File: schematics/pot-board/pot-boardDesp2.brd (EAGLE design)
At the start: 86.4 x 41.9 mm, 15 parts, among them J3 POWER_JACKPTH_LOCK, U1 SPARKFUN_PRO_MICRO, U2 DC-DC-STEP-DOWN-LM2596

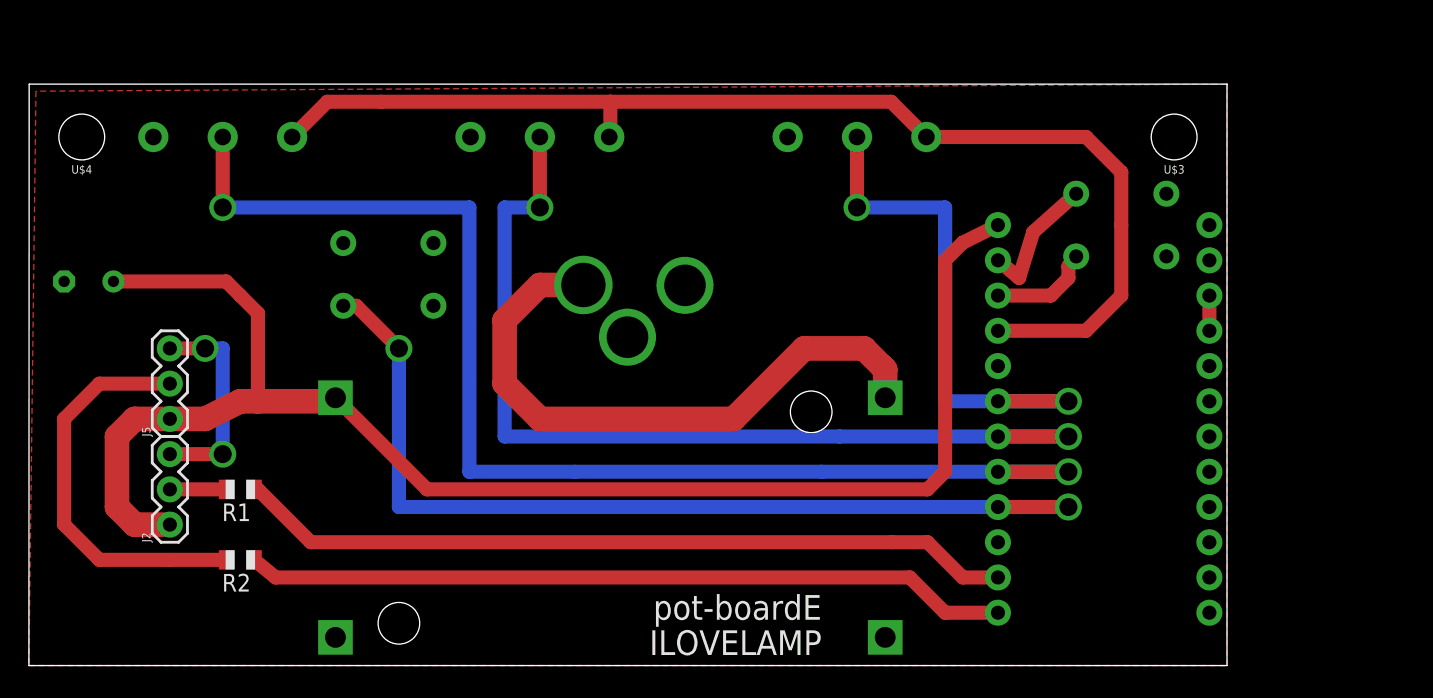
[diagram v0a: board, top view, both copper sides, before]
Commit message: added esp pot boards
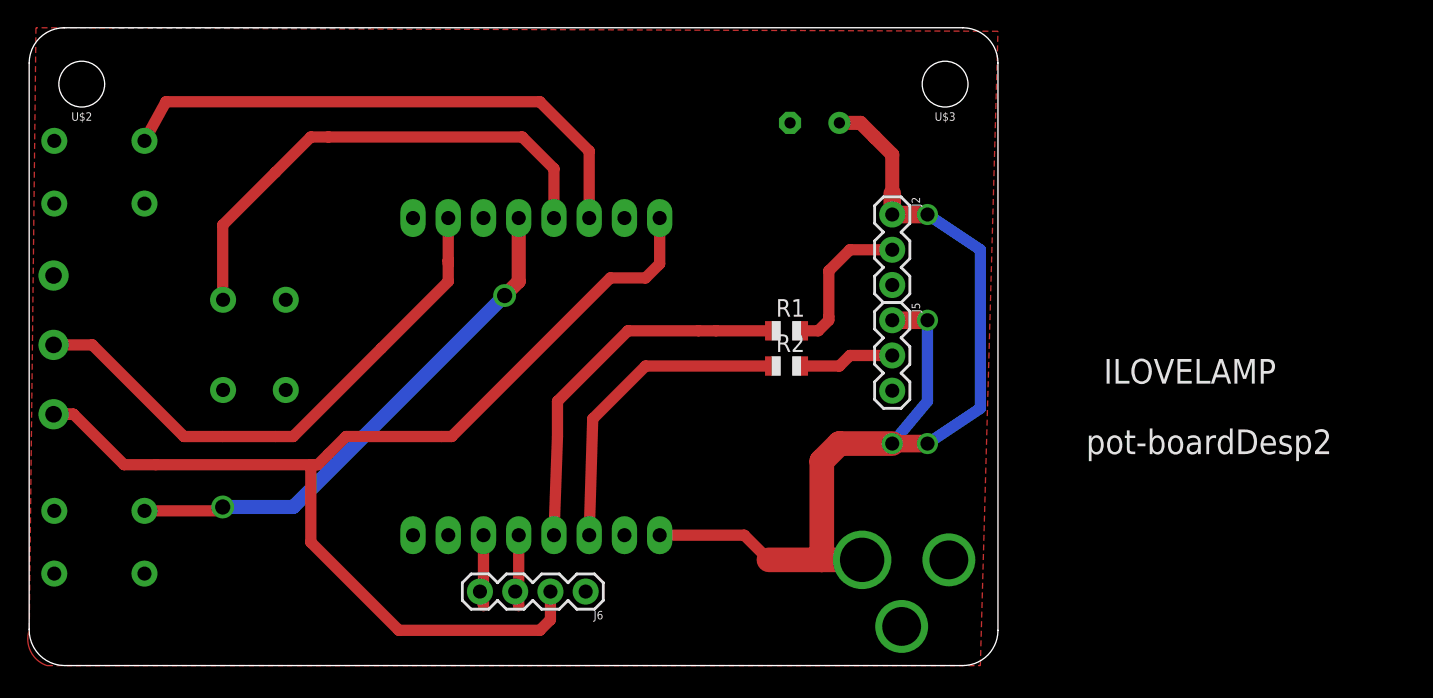
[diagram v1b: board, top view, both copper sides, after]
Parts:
- removed J3: POWER_JACKPTH_LOCK, SparkFun-Connectors:POWER_JACK_PTH_LOCK
- removed R4, R5: (no value), pot:3RP/1610N
- removed S4: tact6mm, SparkFun-Switches:TACTILE_SWITCH_PTH_6.0MM
- removed U$4: (no value), SparkFun-Hardware:STAND-OFF
- removed U1: SPARKFUN_PRO_MICRO, SparkFun-Boards:SPARKFUN_PRO_MICRO
- removed U2: DC-DC-STEP-DOWN-LM2596, diy-modules:DC-DC-STEP-DOWN-LM2596
- added CN1: (no value), adafruit:DCJACK_2MM_PTH
- added J6: (no value), SparkFun-Connectors:1X04
- added S2, S3: tact6mm, SparkFun-Switches:TACTILE_SWITCH_PTH_6.0MM
- added U$2: (no value), SparkFun-Hardware:STAND-OFF
- added WEMOS1: (no value), esp8266modules:WEMOS-D1-MINI
- moved J2 56.7 mm to (62.2, 32.5), turned to 270 degrees
- moved C2 53.6 mm to (56.6, 39.1)
- moved J5 52.6 mm to (62.2, 24.9), turned to 270 degrees
- moved R2 41.8 mm to (54.6, 21.6), turned to 0 degrees
- moved R1 41.0 mm to (54.6, 24.1), turned to 0 degrees
- moved S1 28.4 mm to (5.08, 8.89), turned to 0 degrees
- moved R3 19.3 mm to (1.78, 23.1), turned to 90 degrees
- moved U$3 16.9 mm to (66.0, 41.9)
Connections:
- removed net A1: R4.2, U1.18
- removed net A2: R5.2, U1.19
- removed net N$1: J3.PWR, U2.IN+
- removed net N$5: U1.12
- removed net N$6: U1.15
- removed net RESET: S4.1, U1.22
- removed net RR: U1.7
- removed net VCC: R3.3, R4.3, R5.3, U1.21
- new net +3V3: J6.2, R3.1, WEMOS1.3V3
- new net BUTT2: S2.1, WEMOS1.D6
- new net BUTT3: S3.1, WEMOS1.D7
- net A0: now also WEMOS1.A0; no longer U1.17
- net BUTT1: now also WEMOS1.D5; no longer U1.16
- net GND: now also CN1.GND, CN1.GNDBREAK, J6.1, R3.3, S2.3, S3.3, WEMOS1.GND; no longer J3.GND, J3.GNDBREAK, R3.1, R4.1, R5.1, S4.3, U1.23, U1.3, U1.4, U2.IN-, U2.OUT-
- net LED1: now also WEMOS1.D4; no longer U1.13
- net LED2: now also WEMOS1.D3; no longer U1.14
- net SCL: now also J6.4, WEMOS1.D1; no longer U1.6
- net SDA: now also J6.3, WEMOS1.D2; no longer U1.5
- net VIN: now also CN1.PWR, WEMOS1.5V; no longer U1.24, U2.OUT+
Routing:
- net VCC: track 84.4 -> 0.00 mm
- net +3V3: track 0.00 -> 83.0 mm
- net A1: track 69.9 -> 0.00 mm, vias 2 -> 0
- net A0: track 90.2 -> 40.6 mm, vias 2 -> 0
- net N$1: track 44.6 -> 0.00 mm
- net BUTT3: track 0.00 -> 40.0 mm
- net A2: track 39.4 -> 0.00 mm, vias 2 -> 0
- net BUTT2: track 0.00 -> 36.4 mm
- net VIN: track 113.7 -> 77.7 mm, vias 0 -> 4
- net LED1: track 55.1 -> 22.9 mm
- net BUTT1: track 70.1 -> 38.6 mm
- net LED2: track 56.2 -> 27.3 mm
- net GND: track 27.4 -> 0.00 mm, vias 2 -> 0
- net LED1O: track 29.0 -> 6.94 mm
- net RESET: track 7.35 -> 0.00 mm
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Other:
- board size 86.4 x 41.9 mm -> 69.8 x 46 mm
- board text added: "pot-boardDesp2"
- board text removed: "5V"
- board text removed: "LED1"
- board text removed: "LED2"
- board text removed: "gnd"
- board text removed: "pot-boardE"

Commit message: added woodArc3 sketch
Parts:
- moved S3 0.51 mm to (5.08, 36.1)
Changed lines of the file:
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@@
 <dimension x1="68.58" y1="46.99" x2="0.02" y2="46.99" x3="34.3" y3="62.071209375" textsize="1.778" layer="48" dtype="horizontal" unit="inch" visible="yes"/>
 <dimension x1="-1.504" y1="45.974" x2="0.02" y2="0.33" x3="-14.096875" y3="23.152" textsize="1.778" layer="48" dtype="vertical" unit="inch" visible="yes"/>
-<wire x1="72.644" y1="31.75" x2="-3.556" y2="31.75" width="0" layer="48" style="dashdot"/>
-<wire x1="70.612" y1="12.446" x2="-5.588" y2="12.446" width="0" layer="48" style="dashdot"/>
+<wire x1="71.628" y1="32.766" x2="-4.572" y2="32.766" width="0" layer="48" style="dashdot"/>
+<wire x1="70.358" y1="12.192" x2="-5.842" y2="12.192" width="0" layer="48" style="dashdot"/>
 </plain>
 <attributes>
@@
 <attribute name="PROD_ID" value=" SWCH-08441" x="16.256" y="23.114" size="1.778" layer="28" rot="MR270" display="off"/>
 </element>
-<element name="S3" library="SparkFun-Switches" package="TACTILE_SWITCH_PTH_6.0MM" value="tact6mm" x="5.08" y="35.56" rot="MR0">
-<attribute name="SF_SKU" value="COM-00097" x="5.08" y="35.56" size="1.778" layer="28" rot="MR0" display="off"/>
-<attribute name="PROD_ID" value=" SWCH-08441" x="5.08" y="35.56" size="1.778" layer="28" rot="MR0" display="off"/>
+<element name="S3" library="SparkFun-Switches" package="TACTILE_SWITCH_PTH_6.0MM" value="tact6mm" x="5.08" y="36.068" rot="MR0">
+<attribute name="SF_SKU" value="COM-00097" x="5.08" y="36.068" size="1.778" layer="28" rot="MR0" display="off"/>
+<attribute name="PROD_ID" value=" SWCH-08441" x="5.08" y="36.068" size="1.778" layer="28" rot="MR0" display="off"/>
 </element>
 <element name="CN1" library="adafruit" package="DCJACK_2MM_PTH" value="" x="73.66" y="7.62" rot="MR270"/>
@@
 <wire x1="40.386" y1="37.084" x2="36.83" y2="40.64" width="0.8128" layer="1"/>
 <wire x1="36.83" y1="40.64" x2="9.8806" y2="40.64" width="0.8128" layer="1"/>
-<wire x1="9.8806" y1="40.64" x2="8.3312" y2="37.8206" width="0.8128" layer="1"/>
+<wire x1="8.3312" y1="38.3286" x2="8.3312" y2="39.0906" width="0.8128" layer="1"/>
+<wire x1="8.3312" y1="39.0906" x2="9.8806" y2="40.64" width="0.8128" layer="1"/>
 </signal>
 </signals>
